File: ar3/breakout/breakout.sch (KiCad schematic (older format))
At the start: 2 parts, among them U1 Teensy3.5

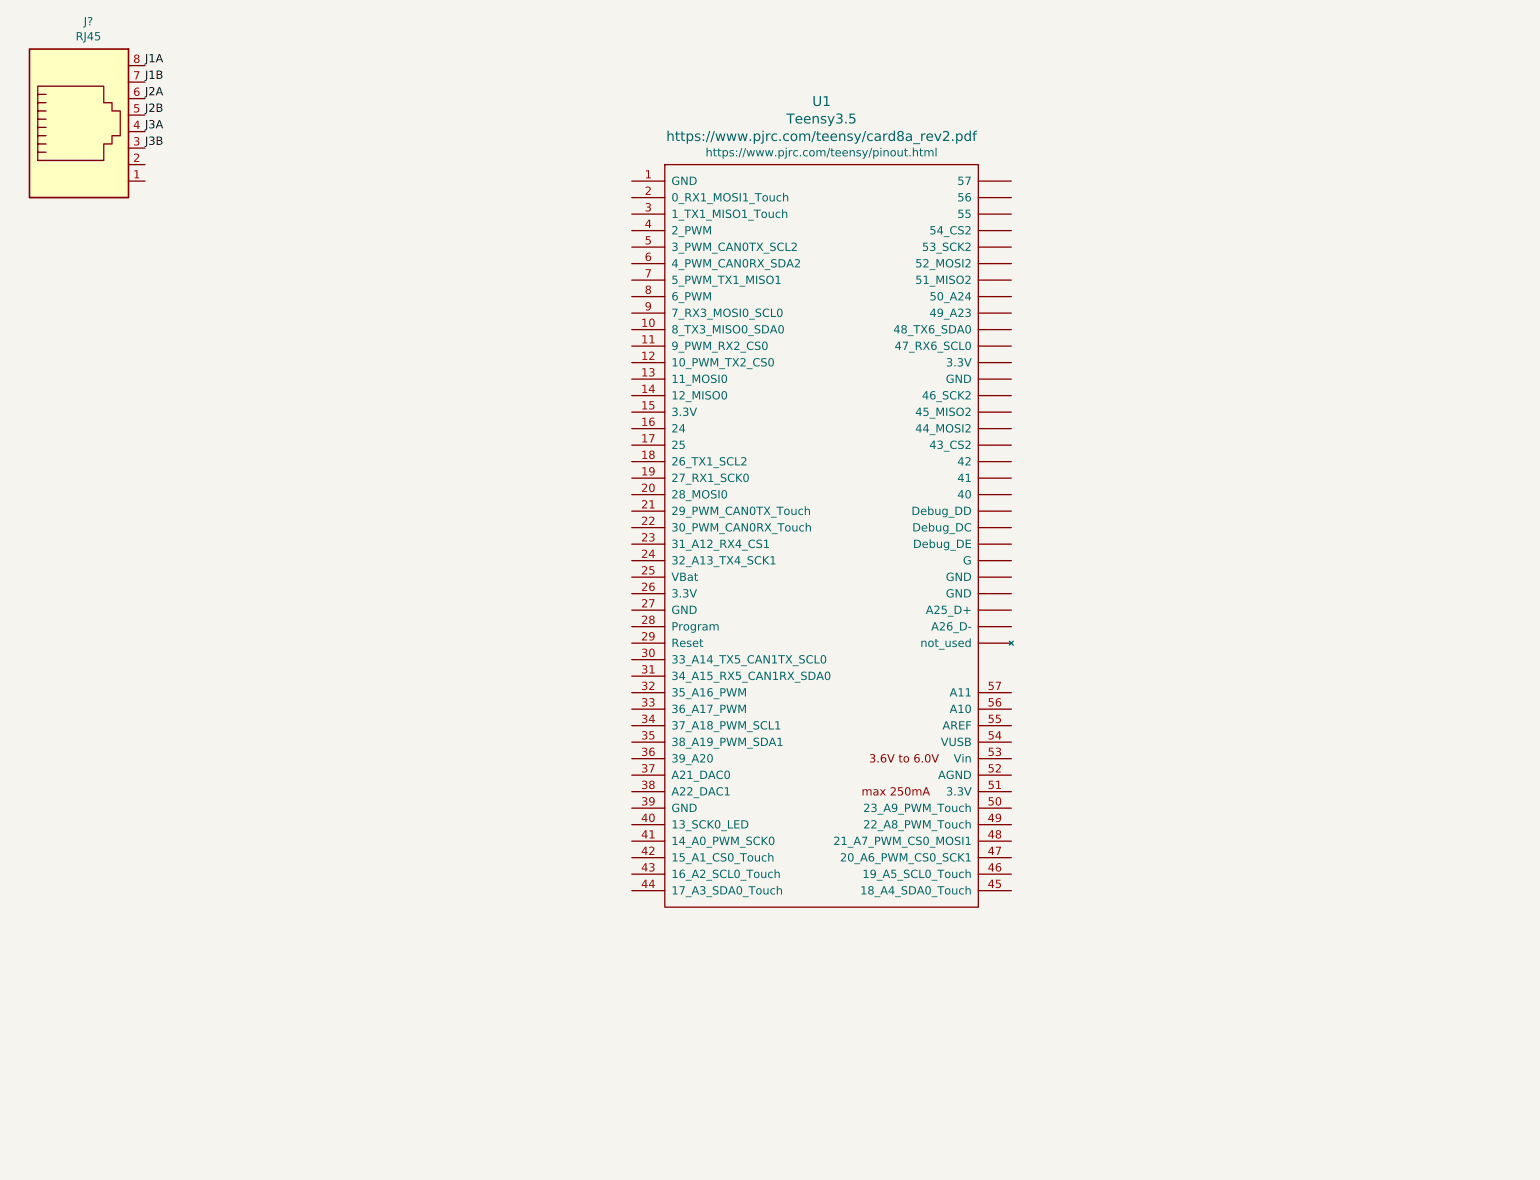
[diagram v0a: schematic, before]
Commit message: Added v1 gerber files for AR3 controller PCB, plus simple arduino encoder code
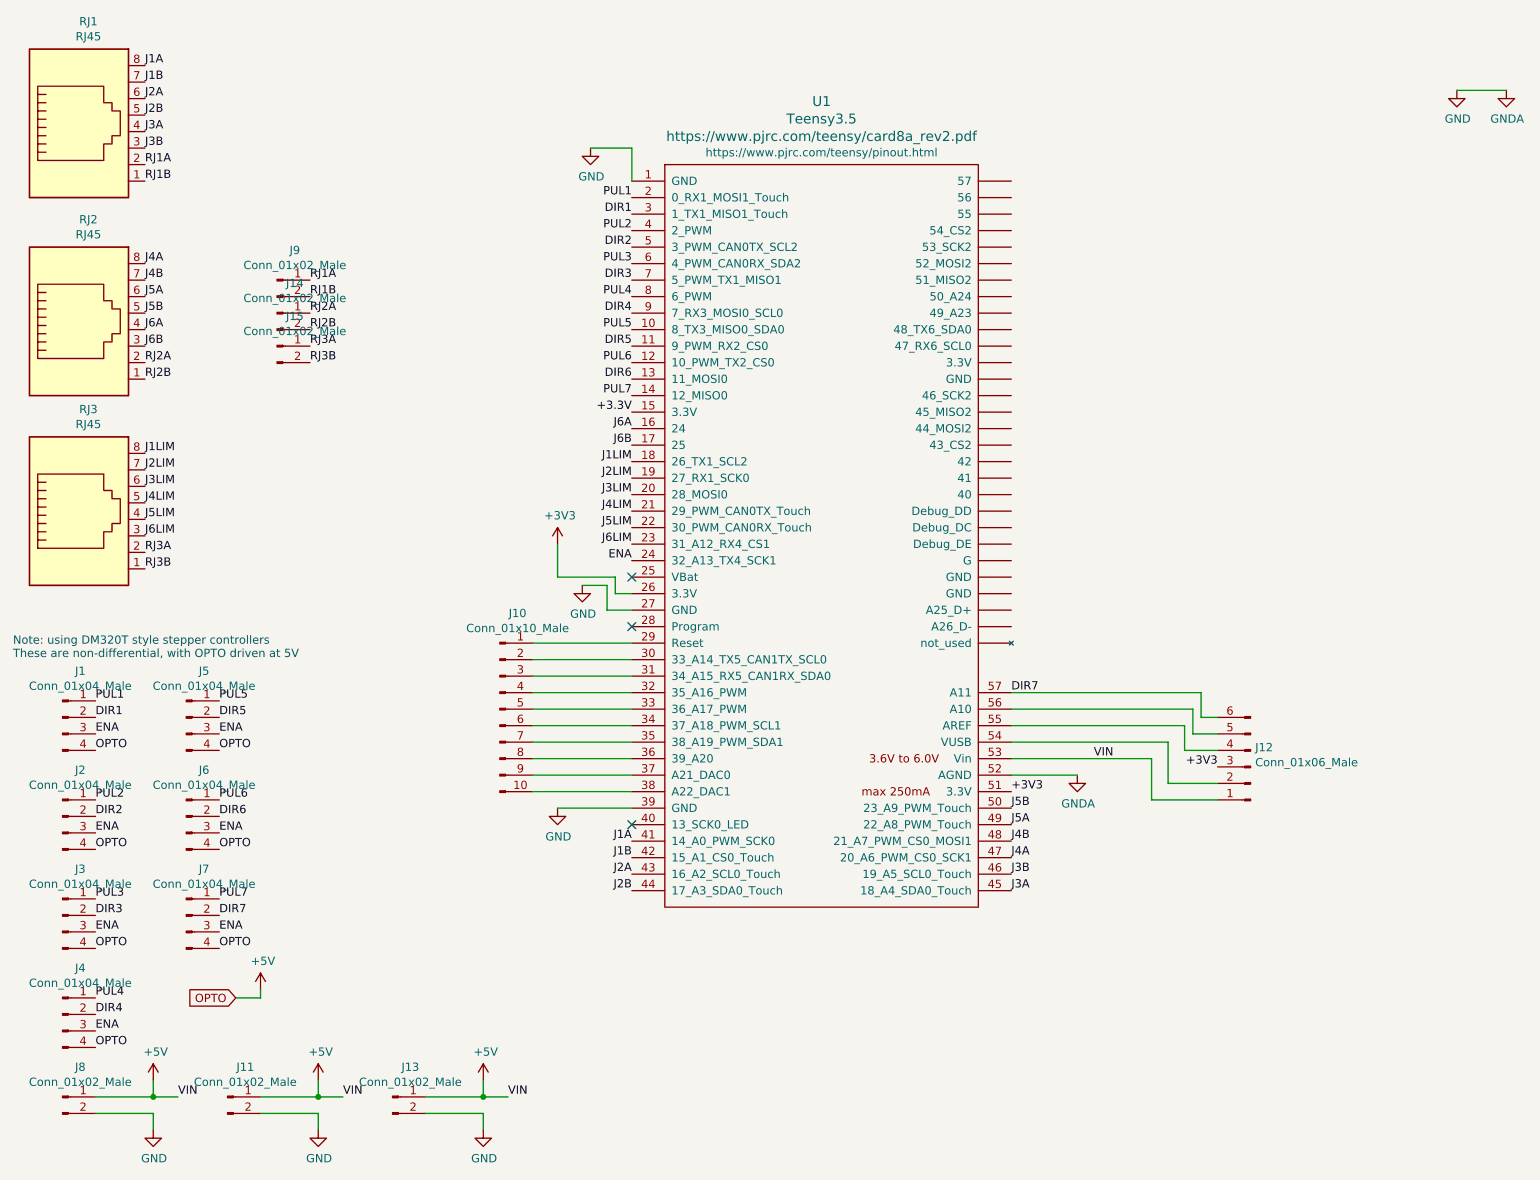
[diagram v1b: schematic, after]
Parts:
- added J1, J2, J3, J4, J5, J6, J7: Conn_01x04_Male, Connector_JST:JST_PH_B4B-PH-K_1x04_P2.00mm_Vertical, symbol Connector:Conn_01x04_Male
- added J10: Conn_01x10_Male, Connector_PinHeader_2.54mm:PinHeader_1x10_P2.54mm_Vertical, symbol Connector:Conn_01x10_Male
- added J11, J13, J14, J15, J8, J9: Conn_01x02_Male, Connector_PinHeader_2.54mm:PinHeader_1x02_P2.54mm_Vertical, symbol Connector:Conn_01x02_Male
- added J12: Conn_01x06_Male, Connector_PinHeader_2.54mm:PinHeader_1x06_P2.54mm_Vertical, symbol Connector:Conn_01x06_Male
- added RJ2, RJ3: RJ45, Connector_RJ:RJ45_Amphenol_54602-x08_Horizontal, symbol Connector:RJ45
- RJ1: renamed from J?; footprint (none) -> Connector_RJ:RJ45_Amphenol_54602-x08_Horizontal
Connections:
- net J1A: now also U1.41 (14_A0_PWM_SCK0)
- net J1B: now also U1.42 (15_A1_CS0_Touch)
- net J2A: now also U1.43 (16_A2_SCL0_Touch)
- net J2B: now also U1.44 (17_A3_SDA0_Touch)
- net J3A: now also U1.45 (18_A4_SDA0_Touch)
- net J3B: now also U1.46 (19_A5_SCL0_Touch)
- net GND: now reaches U1.1 (GND)
- net GND: now also U1.27 (GND), U1.39 (GND), U1.52 (AGND), J11.2 (Pin_2), J13.2 (Pin_2), J8.2 (Pin_2)
- net PUL5: now reaches U1.10 (8_TX3_MISO0_SDA0)
- net PUL5: now also J5.1 (Pin_1)
- net DIR5: now reaches U1.11 (9_PWM_RX2_CS0)
- net DIR5: now also J5.2 (Pin_2)
- net PUL6: now reaches U1.12 (10_PWM_TX2_CS0)
- net PUL6: now also J6.1 (Pin_1)
- net DIR6: now reaches U1.13 (11_MOSI0)
- net DIR6: now also J6.2 (Pin_2)
- net PUL7: now reaches U1.14 (12_MISO0)
- net PUL7: now also J7.1 (Pin_1)
- net +3.3V: now reaches U1.15 (3.3V)
- net J6A: now reaches U1.16 (24)
- net J6A: now also RJ2.4
- net J6B: now reaches U1.17 (25)
- net J6B: now also RJ2.3
- net J1LIM: now reaches U1.18 (26_TX1_SCL2)
- net J1LIM: now also RJ3.8
- net J2LIM: now reaches U1.19 (27_RX1_SCK0)
- net J2LIM: now also RJ3.7
- net PUL1: now reaches U1.2 (0_RX1_MOSI1_Touch)
- net PUL1: now also J1.1 (Pin_1)
- net J3LIM: now reaches U1.20 (28_MOSI0)
- net J3LIM: now also RJ3.6
- net J4LIM: now reaches U1.21 (29_PWM_CAN0TX_Touch)
- net J4LIM: now also RJ3.5
- net J5LIM: now reaches U1.22 (30_PWM_CAN0RX_Touch)
- net J5LIM: now also RJ3.4
- net J6LIM: now reaches U1.23 (31_A12_RX4_CS1)
- net J6LIM: now also RJ3.3
- net ENA: now reaches U1.24 (32_A13_TX4_SCK1)
- net ENA: now also J1.3 (Pin_3), J2.3 (Pin_3), J3.3 (Pin_3), J4.3 (Pin_3), J5.3 (Pin_3), J6.3 (Pin_3), J7.3 (Pin_3)
- net +3V3: now reaches U1.26 (3.3V)
- net +3V3: now also U1.51 (3.3V), J12.3 (Pin_3)
- net at U1.29 (Reset): now also J10.1 (Pin_1)
- net DIR1: now reaches U1.3 (1_TX1_MISO1_Touch)
- net DIR1: now also J1.2 (Pin_2)
- net at U1.30 (33_A14_TX5_CAN1TX_SCL0): now also J10.2 (Pin_2)
- net at U1.31 (34_A15_RX5_CAN1RX_SDA0): now also J10.3 (Pin_3)
- net at U1.32 (35_A16_PWM): now also J10.4 (Pin_4)
- net at U1.33 (36_A17_PWM): now also J10.5 (Pin_5)
- net at U1.34 (37_A18_PWM_SCL1): now also J10.6 (Pin_6)
- net at U1.35 (38_A19_PWM_SDA1): now also J10.7 (Pin_7)
- net at U1.36 (39_A20): now also J10.8 (Pin_8)
- net at U1.37 (A21_DAC0): now also J10.9 (Pin_9)
- net at U1.38 (A22_DAC1): now also J10.10 (Pin_10)
- net PUL2: now reaches U1.4 (2_PWM)
- net PUL2: now also J2.1 (Pin_1)
- net J4A: now reaches U1.47 (20_A6_PWM_CS0_SCK1)
- net J4A: now also RJ2.8
- net J4B: now reaches U1.48 (21_A7_PWM_CS0_MOSI1)
- net J4B: now also RJ2.7
- net J5A: now reaches U1.49 (22_A8_PWM_Touch)
- net J5A: now also RJ2.6
- net DIR2: now reaches U1.5 (3_PWM_CAN0TX_SCL2)
- net DIR2: now also J2.2 (Pin_2)
- net J5B: now reaches U1.50 (23_A9_PWM_Touch)
- net J5B: now also RJ2.5
- net +5V: now reaches U1.53 (Vin)
- net +5V: now also J1.4 (Pin_4), J11.1 (Pin_1), J12.1 (Pin_1), J13.1 (Pin_1), J2.4 (Pin_4), J3.4 (Pin_4), J4.4 (Pin_4), J5.4 (Pin_4), J6.4 (Pin_4), J7.4 (Pin_4), J8.1 (Pin_1)
- net at U1.54 (VUSB): now also J12.2 (Pin_2)
- net at U1.55 (AREF): now also J12.4 (Pin_4)
- net at U1.56 (A10): now also J12.5 (Pin_5)
- net DIR7: now reaches U1.57 (A11)
- net DIR7: now also J12.6 (Pin_6), J7.2 (Pin_2)
- net PUL3: now reaches U1.6 (4_PWM_CAN0RX_SDA2)
- net PUL3: now also J3.1 (Pin_1)
- net DIR3: now reaches U1.7 (5_PWM_TX1_MISO1)
- net DIR3: now also J3.2 (Pin_2)
- net PUL4: now reaches U1.8 (6_PWM)
- net PUL4: now also J4.1 (Pin_1)
- net DIR4: now reaches U1.9 (7_RX3_MOSI0_SCL0)
- net DIR4: now also J4.2 (Pin_2)
- net RJ1B: now reaches RJ1.1
- net RJ1B: now also J9.2 (Pin_2)
- net RJ1A: now reaches RJ1.2
- net RJ1A: now also J9.1 (Pin_1)
- new net RJ2A: J14.1 (Pin_1), RJ2.2
- new net RJ2B: J14.2 (Pin_2), RJ2.1
- new net RJ3A: J15.1 (Pin_1), RJ3.2
- new net RJ3B: J15.2 (Pin_2), RJ3.1
- no-connect marks 0 -> 3
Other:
- note added: "Note: using DM320T style stepper controllers\nThese are non-differential, with OPTO driven at 5V"

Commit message: Added TODOs to AR3 breakout schematic
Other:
- note added: "TODO\nConfigurable 5V / 24V logic shifter (stepper drivers)\nSeparatable power via jumper\n6x RS422 line receiver channels to read encoders w/ differential signal"
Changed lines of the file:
@@
 	3550 7150 3700 7150
 Connection ~ 3550 7150
+Text Notes 2750 3550 0    394  ~ 0
+TODO\nConfigurable 5V / 24V logic shifter (stepper drivers)\nSeparatable power via jumper\n6x RS422 line receiver channels to read encoders w/ differential signal
 $EndSCHEMATC
